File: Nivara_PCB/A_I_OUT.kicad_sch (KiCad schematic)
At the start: 19 parts, among them U4 AP63200WU

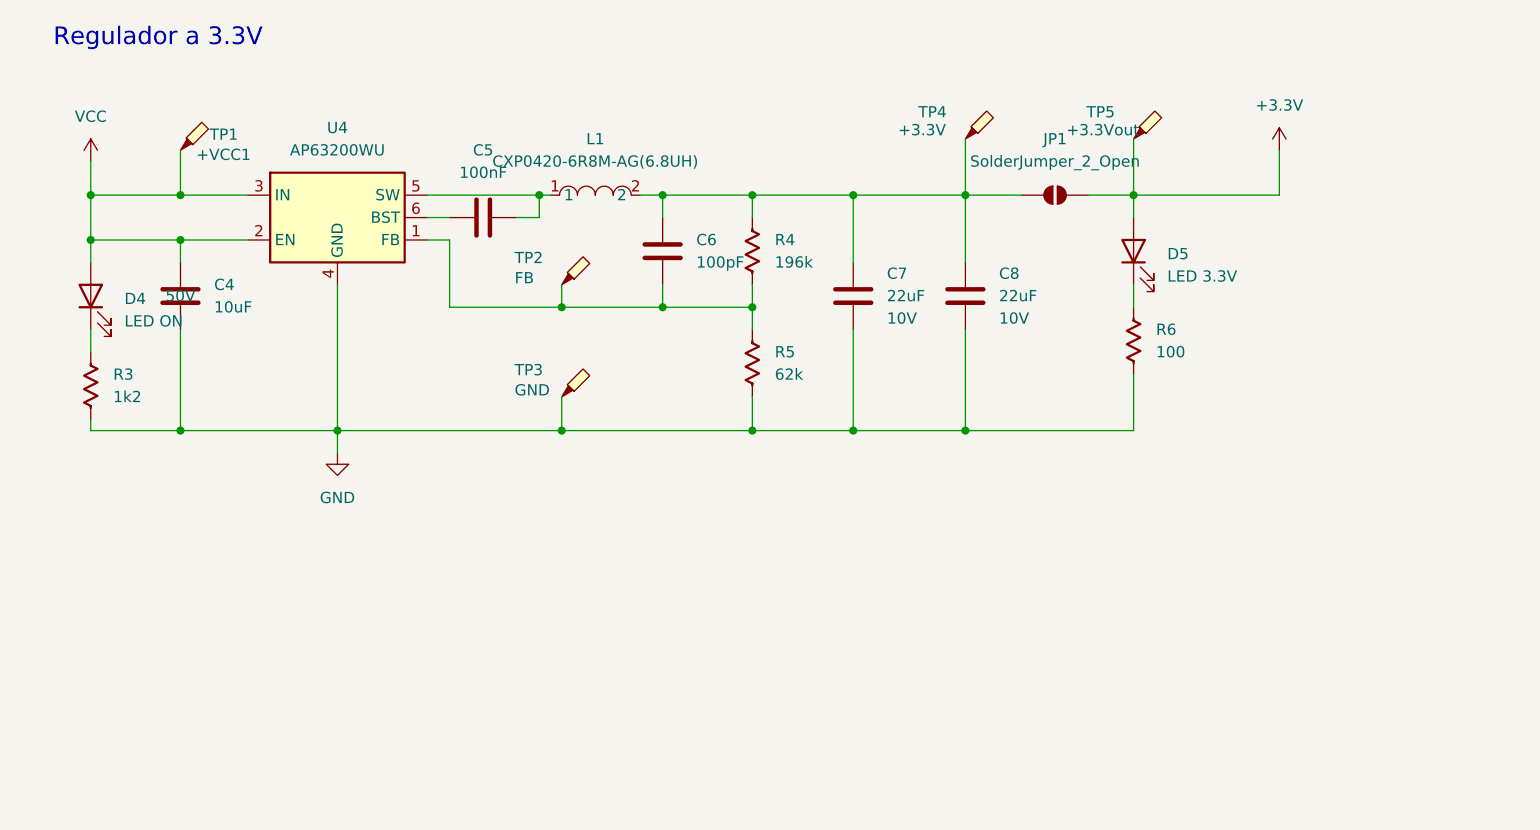
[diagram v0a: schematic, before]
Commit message: Cambios realizados en el PCB y el esquema de Nivara_PCB.
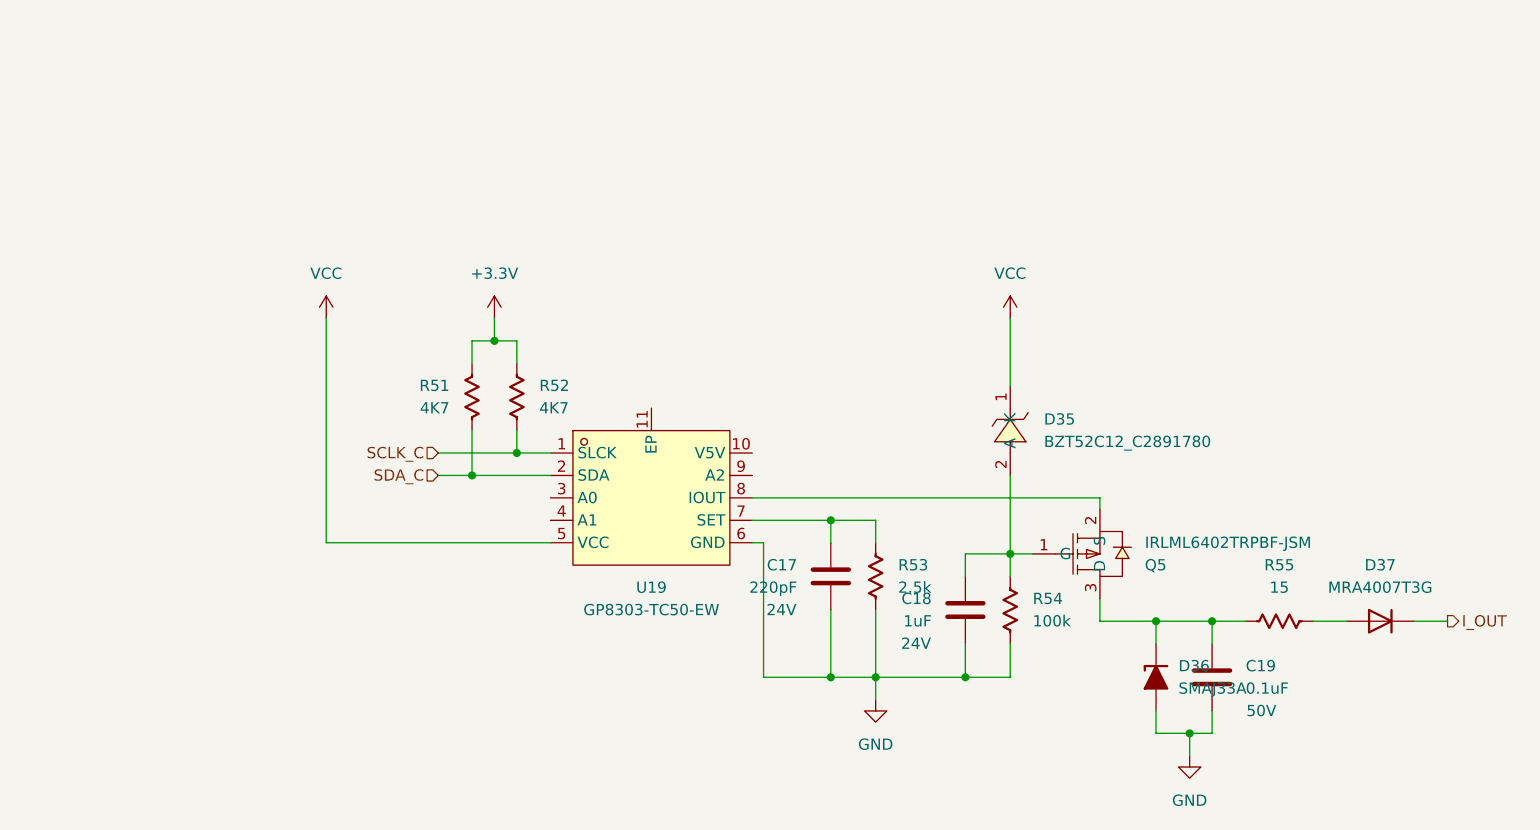
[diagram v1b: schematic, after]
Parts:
- removed C4: 10uF, PCM_Capacitor_SMD_AKL:C_1206_3216Metric, symbol PCM_Capacitor_AKL:C_1206
- removed C5: 100nF, PCM_Capacitor_SMD_AKL:C_0805_2012Metric, symbol PCM_Capacitor_AKL:C_0805
- removed C6: 100pF, PCM_Capacitor_SMD_AKL:C_0805_2012Metric, symbol PCM_Capacitor_AKL:C_0805
- removed C7, C8: 22uF, PCM_Capacitor_SMD_AKL:C_0603_1608Metric, symbol PCM_Capacitor_AKL:C_0603
- removed D4: LED ON, LED_SMD:LED_0603_1608Metric, symbol Device:LED
- removed D5: LED 3.3V, LED_SMD:LED_0603_1608Metric, symbol Device:LED
- removed JP1: SolderJumper_2_Open, Jumper:SolderJumper-2_P1.3mm_Open_Pad1.0x1.5mm, symbol Jumper:SolderJumper_2_Open
- removed L1: CXP0420-6R8M-AG(6.8UH), EasyEDA:IND-SMD_L4.4-W4.2_CXP0420, symbol EasyEDA:CXP0420-6R8M-AG(6.8UH)
- removed R3: 1k2, PCM_Resistor_SMD_AKL:R_0603_1608Metric, symbol PCM_Resistor_US_AKL:R_0603
- removed R4: 196k, PCM_Resistor_SMD_AKL:R_0603_1608Metric, symbol PCM_Resistor_US_AKL:R_0603
- removed R5: 62k, PCM_Resistor_SMD_AKL:R_0603_1608Metric, symbol PCM_Resistor_US_AKL:R_0603
- removed R6: 100, PCM_Resistor_SMD_AKL:R_0603_1608Metric, symbol PCM_Resistor_US_AKL:R_0603
- removed TP1: +VCC1, TestPoint:TestPoint_Pad_1.0x1.0mm, symbol Connector:TestPoint_Probe
- removed TP2: FB, TestPoint:TestPoint_Pad_1.0x1.0mm, symbol Connector:TestPoint_Probe
- removed TP3: GND, TestPoint:TestPoint_Pad_1.0x1.0mm, symbol Connector:TestPoint_Probe
- removed TP4: +3.3V, TestPoint:TestPoint_Pad_1.0x1.0mm, symbol Connector:TestPoint_Probe
- removed TP5: +3.3Vout, TestPoint:TestPoint_Pad_1.0x1.0mm, symbol Connector:TestPoint_Probe
- removed U4: AP63200WU, Package_TO_SOT_SMD:TSOT-23-6, symbol Regulator_Switching:AP63200WU
- added C17: 220pF, PCM_Capacitor_SMD_AKL:C_0603_1608Metric, symbol PCM_Capacitor_US_AKL:C_0603
- added C18: 1uF, PCM_Capacitor_SMD_AKL:C_0603_1608Metric, symbol PCM_Capacitor_US_AKL:C_0603
- added C19: 0.1uF, PCM_Capacitor_SMD_AKL:C_0603_1608Metric, symbol PCM_Capacitor_US_AKL:C_0603
- added D35: BZT52C12_C2891780, EasyEDA:SOD-123_L2.7-W1.6-LS3.7-RD-1, symbol EasyEDA:BZT52C12_C2891780
- added D36: SMAJ33A, PCM_Diode_SMD_AKL:D_SMA, symbol PCM_Diode_TVS_AKL:SMAJ33A
- added D37: MRA4007T3G, Diode_SMD:D_SMA, symbol Diode:MRA4007T3G
- added Q5: IRLML6402TRPBF-JSM, EasyEDA:SOT-23-3_L2.9-W1.3-P1.90-LS2.4-BR, symbol EasyEDA:IRLML6402TRPBF-JSM
- added R51, R52: 4K7, PCM_Resistor_SMD_AKL:R_0603_1608Metric, symbol PCM_Resistor_US_AKL:R_0603
- added R53: 2.5k, PCM_Resistor_SMD_AKL:R_0603_1608Metric, symbol PCM_Resistor_US_AKL:R_0603
- added R54: 100k, PCM_Resistor_SMD_AKL:R_0603_1608Metric, symbol PCM_Resistor_US_AKL:R_0603
- added R55: 15, PCM_Resistor_SMD_AKL:R_0805_2012Metric, symbol PCM_Resistor_US_AKL:R_0805
- added U19: GP8303-TC50-EW, EasyEDA:ESOP-10_L4.9-W3.9-P1.00-LS6.1-BL-EP, symbol EasyEDA:GP8303-TC50-EW
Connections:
- net +3.3V: now also R51.1, R52.1
- net GND: now also C17.2, C18.2, C19.2, D36.2 (A), R53.2, R54.2, U19.6 (GND)
- net VCC: now also D35.1 (K), U19.5 (VCC)
- new net: C17.1, R53.1, U19.7 (SET)
- new net: C18.1, D35.2 (A), Q5.1 (G), R54.1
- new net: C19.1, D36.1 (K), Q5.3 (D), R55.1
- new net: Q5.2 (S), U19.8 (IOUT)
- new net: D37.2 (A), R55.2
- new net I_OUT: D37.1 (K)
- new net SCLK_C: R52.2, U19.1 (SLCK)
- new net SDA_C: R51.2, U19.2 (SDA)
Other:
- note removed: "Regulador a 3.3V"

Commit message: Cambios realizados en los archivos de Nivara_PCB.
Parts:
- C17, C18, C19: symbol PCM_Capacitor_US_AKL:C_0603 -> EasyEDA:C_0603
- D36: symbol PCM_Diode_TVS_AKL:SMAJ33A -> EasyEDA:SMAJ33A
- D37: symbol Diode:MRA4007T3G -> EasyEDA:MRA4007T3G
- R51, R52, R53, R54: symbol PCM_Resistor_US_AKL:R_0603 -> EasyEDA:R_0603
- R55: symbol PCM_Resistor_US_AKL:R_0805 -> EasyEDA:R_0805
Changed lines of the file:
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@@
 	)
 	(symbol
-		(lib_id "PCM_Capacitor_US_AKL:C_0603")
+		(lib_id "EasyEDA:C_0603")
 		(at 127 90.17 0)
 		(mirror y)
@@
 	)
 	(symbol
-		(lib_id "power:VCC")
+		(lib_id "EasyEDA:VCC")
 		(at 147.32 60.96 0)
 		(unit 1)
@@
 	)
 	(symbol
-		(lib_id "PCM_Capacitor_US_AKL:C_0603")
+		(lib_id "EasyEDA:C_0603")
 		(at 142.24 93.98 0)
 		(mirror y)
@@
 	)
 	(symbol
-		(lib_id "power:+3.3V")
+		(lib_id "EasyEDA:+3.3V")
 		(at 88.9 60.96 0)
 		(unit 1)
@@
 	)
 	(symbol
-		(lib_id "PCM_Diode_TVS_AKL:SMAJ33A")
+		(lib_id "EasyEDA:SMAJ33A")
 		(at 163.83 101.6 90)
 		(unit 1)
@@
 	)
 	(symbol
-		(lib_id "power:GND")
+		(lib_id "EasyEDA:GND")
 		(at 132.08 104.14 0)
 		(unit 1)
@@
 	)
 	(symbol
-		(lib_id "Diode:MRA4007T3G")
+		(lib_id "EasyEDA:MRA4007T3G")
 		(at 189.23 95.25 0)
 		(mirror y)
@@
 	)
 	(symbol
-		(lib_id "power:VCC")
+		(lib_id "EasyEDA:VCC")
 		(at 69.85 60.96 0)
 		(unit 1)
@@
 	)
 	(symbol
-		(lib_id "PCM_Resistor_US_AKL:R_0603")
+		(lib_id "EasyEDA:R_0603")
 		(at 91.44 69.85 0)
 		(unit 1)
@@
 	)
 	(symbol
-		(lib_id "PCM_Resistor_US_AKL:R_0603")
+		(lib_id "EasyEDA:R_0603")
 		(at 86.36 69.85 0)
 		(mirror y)
@@
 	)
 	(symbol
-		(lib_id "PCM_Resistor_US_AKL:R_0603")
+		(lib_id "EasyEDA:R_0603")
 		(at 147.32 93.98 0)
 		(unit 1)
@@
 	)
 	(symbol
-		(lib_id "PCM_Capacitor_US_AKL:C_0603")
+		(lib_id "EasyEDA:C_0603")
 		(at 170.18 101.6 0)
 		(unit 1)
@@
 	)
 	(symbol
-		(lib_id "PCM_Resistor_US_AKL:R_0603")
+		(lib_id "EasyEDA:R_0603")
 		(at 132.08 90.17 0)
 		(unit 1)
@@
 	)
 	(symbol
-		(lib_id "PCM_Resistor_US_AKL:R_0805")
+		(lib_id "EasyEDA:R_0805")
 		(at 177.8 95.25 90)
 		(unit 1)
@@
 	)
 	(symbol
-		(lib_id "power:GND")
+		(lib_id "EasyEDA:GND")
 		(at 167.64 110.49 0)
 		(unit 1)
